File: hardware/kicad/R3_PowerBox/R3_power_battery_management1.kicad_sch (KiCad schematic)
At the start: 22 parts, among them J8 2S BATTERY / KEYED, J9 CHARGER NTC / OPTIONAL, Q2 20V N-MOS LOW-RDS / MPN TBD, Q3 20V N-MOS LOW-RDS / MPN TBD, U9 BQ28Z610DRZR

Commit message: Finalize R3 PowerBox pre-placement corrections
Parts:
- added C95: 100nF DSG D-S / TI EVM, Capacitor_SMD:C_0603_1608Metric, symbol R3_POWER_GEN:C
- added C96: 100nF CHG D-S / TI EVM, Capacitor_SMD:C_0603_1608Metric, symbol R3_POWER_GEN:C
- added C97: 100nF VC2-VC1 / CELL2, Capacitor_SMD:C_0603_1608Metric, symbol R3_POWER_GEN:C
- added C98: 100nF VC1-VSS / CELL1, Capacitor_SMD:C_0603_1608Metric, symbol R3_POWER_GEN:C
- added R100: 5.1k CHG GATE / TI EVM, Resistor_SMD:R_0603_1608Metric, symbol R3_POWER_GEN:R
- added R101: 10M CHG G-S / TI EVM, Resistor_SMD:R_0603_1608Metric, symbol R3_POWER_GEN:R
- added R98: 5.1k DSG GATE / TI EVM, Resistor_SMD:R_0603_1608Metric, symbol R3_POWER_GEN:R
- added R99: 10M DSG G-S / TI EVM, Resistor_SMD:R_0603_1608Metric, symbol R3_POWER_GEN:R
- added U11: BQ294502 SPACE ONLY / NC / DNP, Package_SON:WSON-6-1EP_2x2mm_P0.65mm_EP1x1.6mm, symbol Connector_Generic:Conn_01x07
- J9: value CHARGER NTC / OPTIONAL -> CHARGER NTC / QUIET DGND RETURN
- Q2: value 20V N-MOS LOW-RDS / MPN TBD -> 30V N-MOS DSG / MPN+FOOTPRINT TBD
- Q3: value 20V N-MOS LOW-RDS / MPN TBD -> 30V N-MOS CHG / MPN+FOOTPRINT TBD
- R90: value 100R VC2 -> 100R VC2 / KELVIN
- R91: value 100R VC1 -> 100R VC1 / KELVIN
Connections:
- net BAT_NEG_RAW: now also C98.2; no longer J9.2
- net BAT_POS_RAW: now also Q3.2 (S), C96.2, R101.2; no longer Q2.3 (D)
- net BMS_FET_COMMON: now also Q2.3 (D), Q3.3 (D), C95.2, C96.1; no longer Q2.2 (S), Q3.2 (S)
- net BMS_VC2_FILT: now also C97.1
- net DGND: now also J9.2
- net N$1: now also R92.2, U9.4 (TS1); no longer R91.2, U9.12 (VC1)
- net N$2: now also U9.7 (DSG), R98.1; no longer R92.2, U9.4 (TS1)
- net N$3: now also R100.1; no longer Q2.1 (G)
- net PACK_POS: now also Q2.2 (S), C95.1, R99.2; no longer Q3.3 (D)
- net N$4 renamed BMS_CHG_GATE
- net BMS_CHG_GATE: now also R100.2, R101.1; no longer U9.7 (DSG)
- new net BMS_DSG_GATE: Q2.1 (G), R98.2, R99.1
- new net BMS_VC1_FILT: C97.2, C98.1, R91.2, U9.12 (VC1)
- no-connect marks 0 -> 7
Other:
- moved on the sheet: C93, C94, J8, J9, Q2, Q3, R90, R91, R92, R93, R94, R95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

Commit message: Finalize R3 PowerBox pre-routing placement
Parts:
- J8: value 2S BATTERY / KEYED -> 2S BATTERY / KEYED / NTC_BMS=103AT-2
- J9: value CHARGER NTC / QUIET DGND RETURN -> NTC_CHG=103AT-2 / QUIET DGND RETURN
- Q2: value 30V N-MOS DSG / MPN+FOOTPRINT TBD -> CSD17577Q3AT 30V NMOS DSG; footprint (none) -> R3_Power:CSD17577Q3A_VSON-8_3.3x3.3mm
- Q3: value 30V N-MOS CHG / MPN+FOOTPRINT TBD -> CSD17577Q3AT 30V NMOS CHG; footprint (none) -> R3_Power:CSD17577Q3A_VSON-8_3.3x3.3mm
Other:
- moved on the sheet: R90, R96, R97

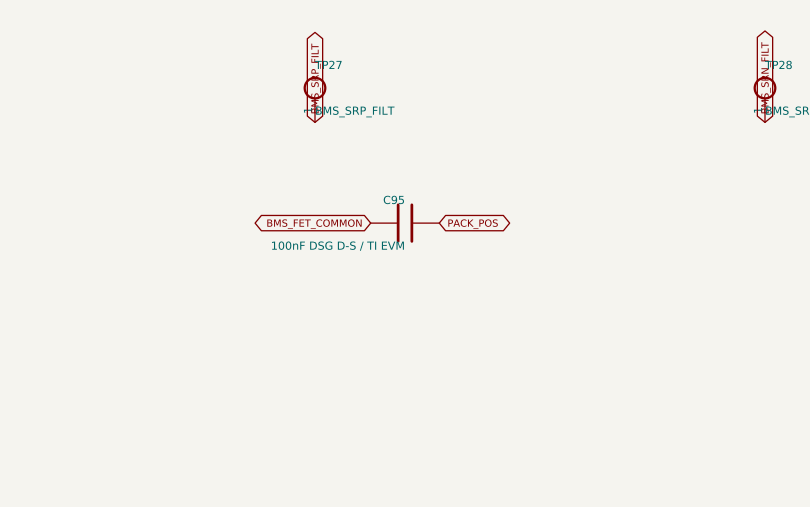
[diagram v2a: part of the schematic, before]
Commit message: Finalize R3 PowerBox user power controls
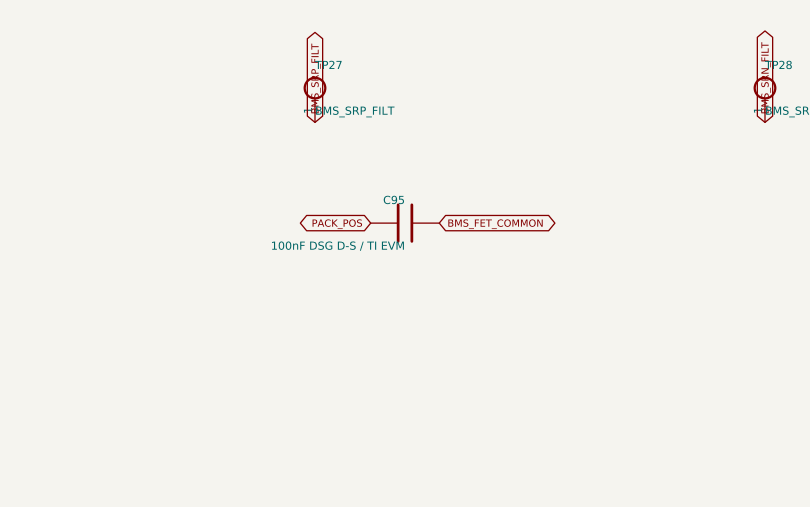
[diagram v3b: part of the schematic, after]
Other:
- moved on the sheet: C95

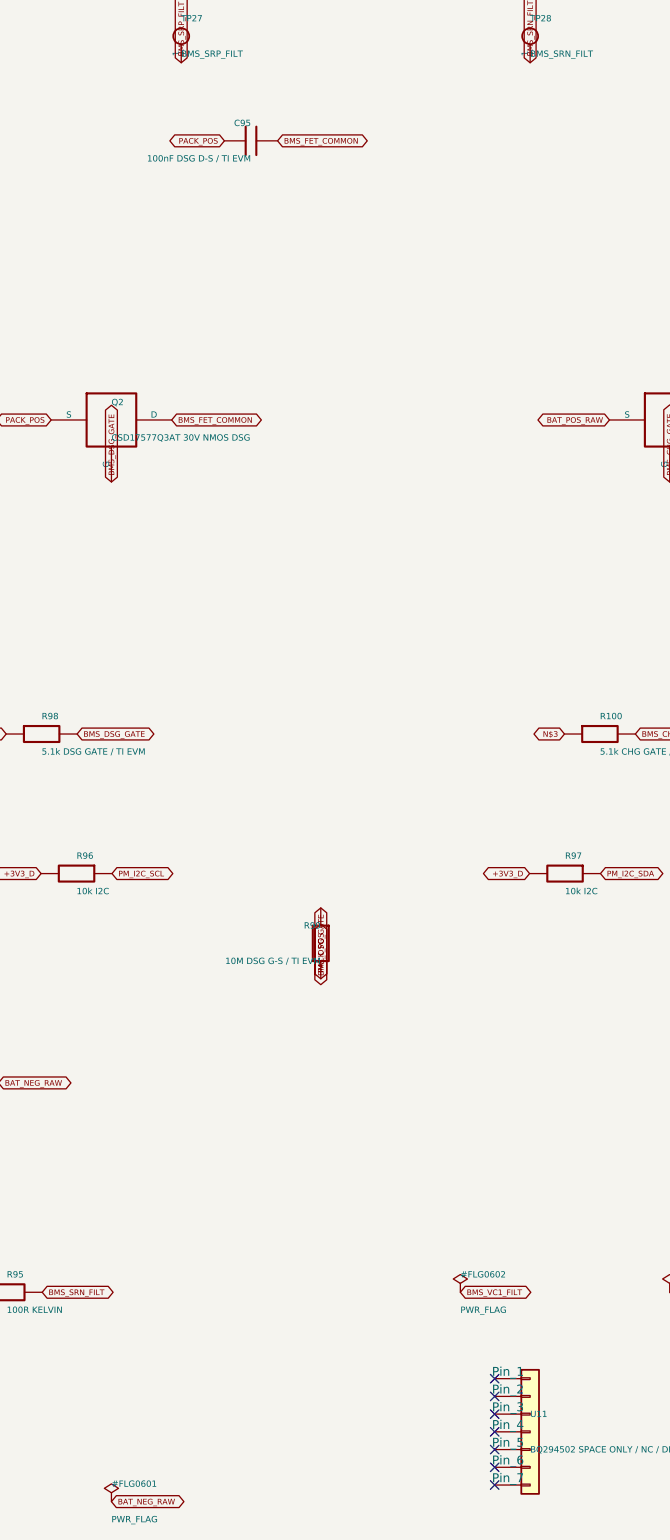
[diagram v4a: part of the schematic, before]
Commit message: Finish R3 PowerBox routing checkpoint F and verification
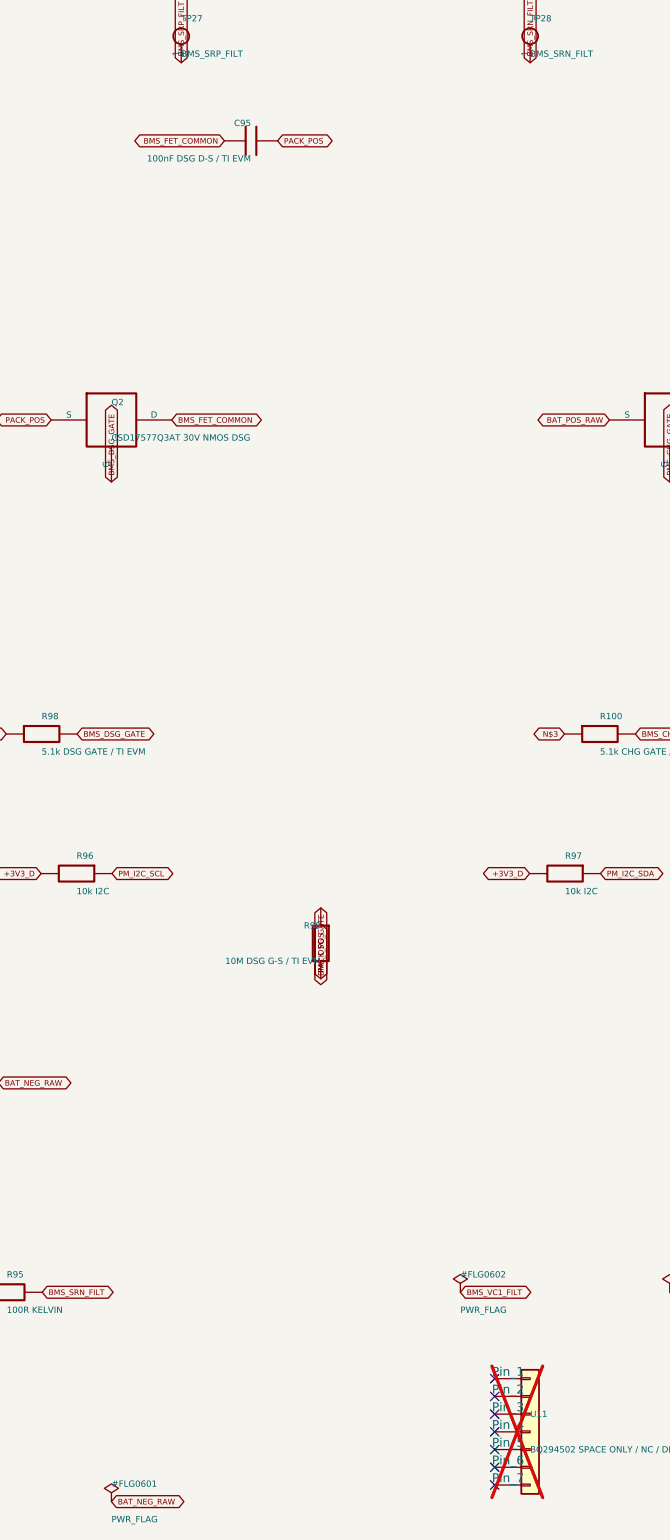
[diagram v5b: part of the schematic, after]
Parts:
- TP27, TP28: footprint TestPoint:TestPoint_Plated_Hole_D2.0mm -> TestPoint:TestPoint_Pad_D1.0mm
- U11: now not fitted
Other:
- moved on the sheet: C95

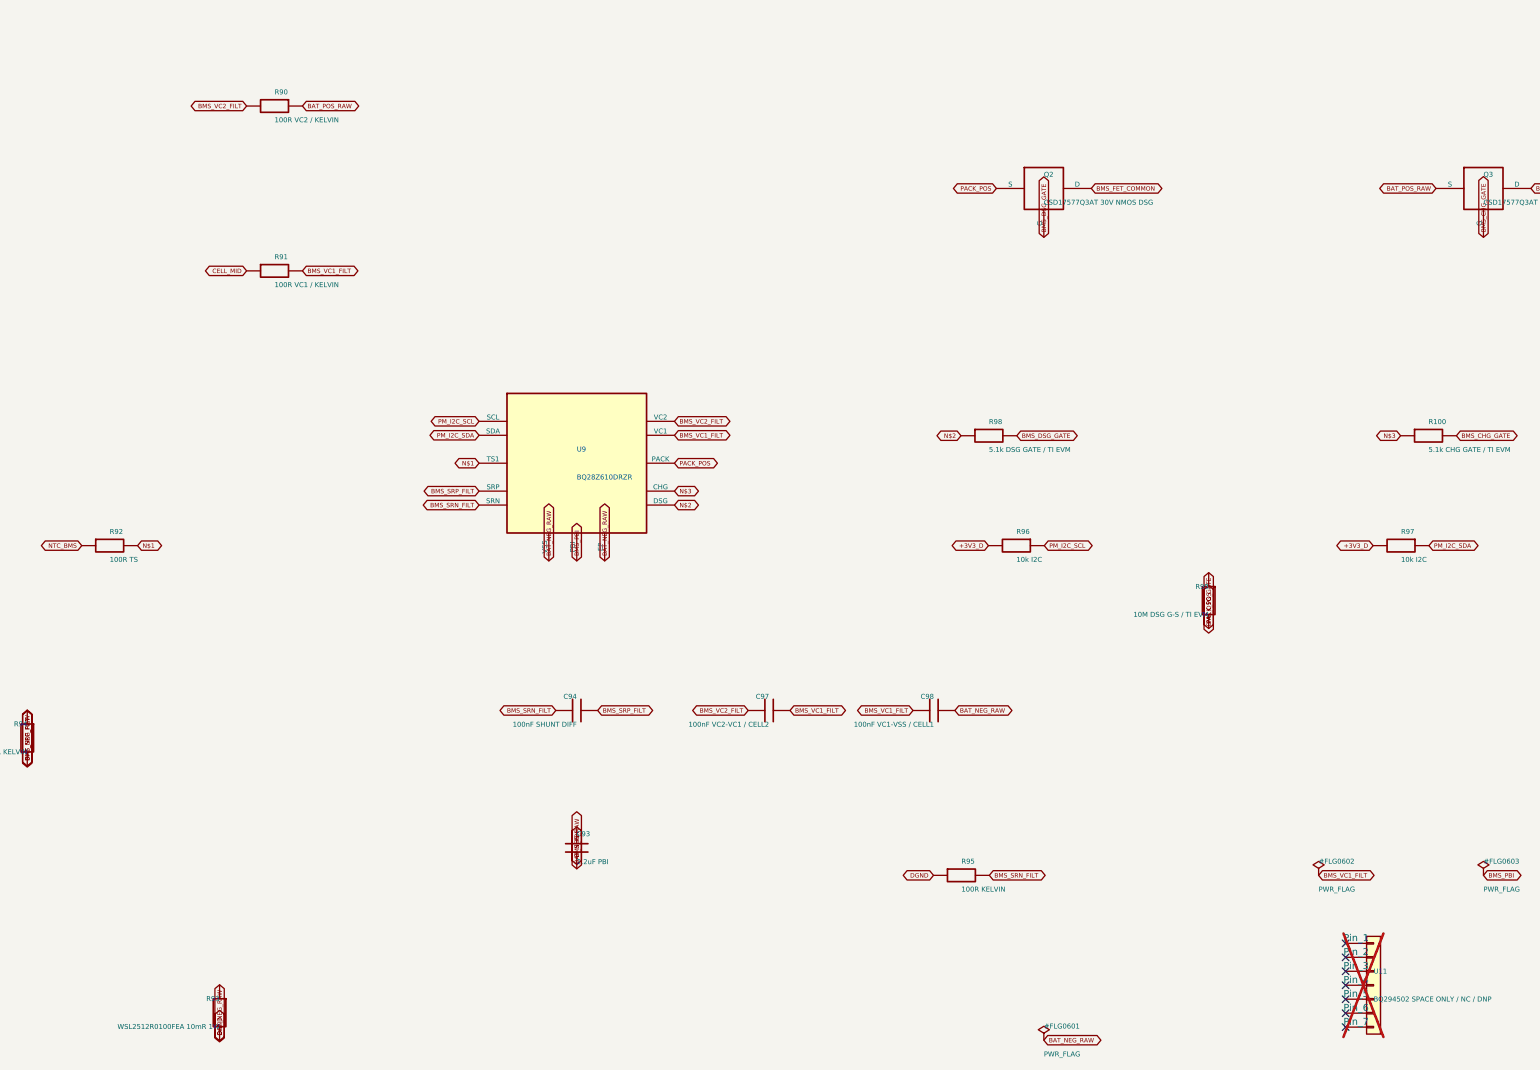
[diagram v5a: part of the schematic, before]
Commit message: Rev.A review fixes: initial schematic and component corrections
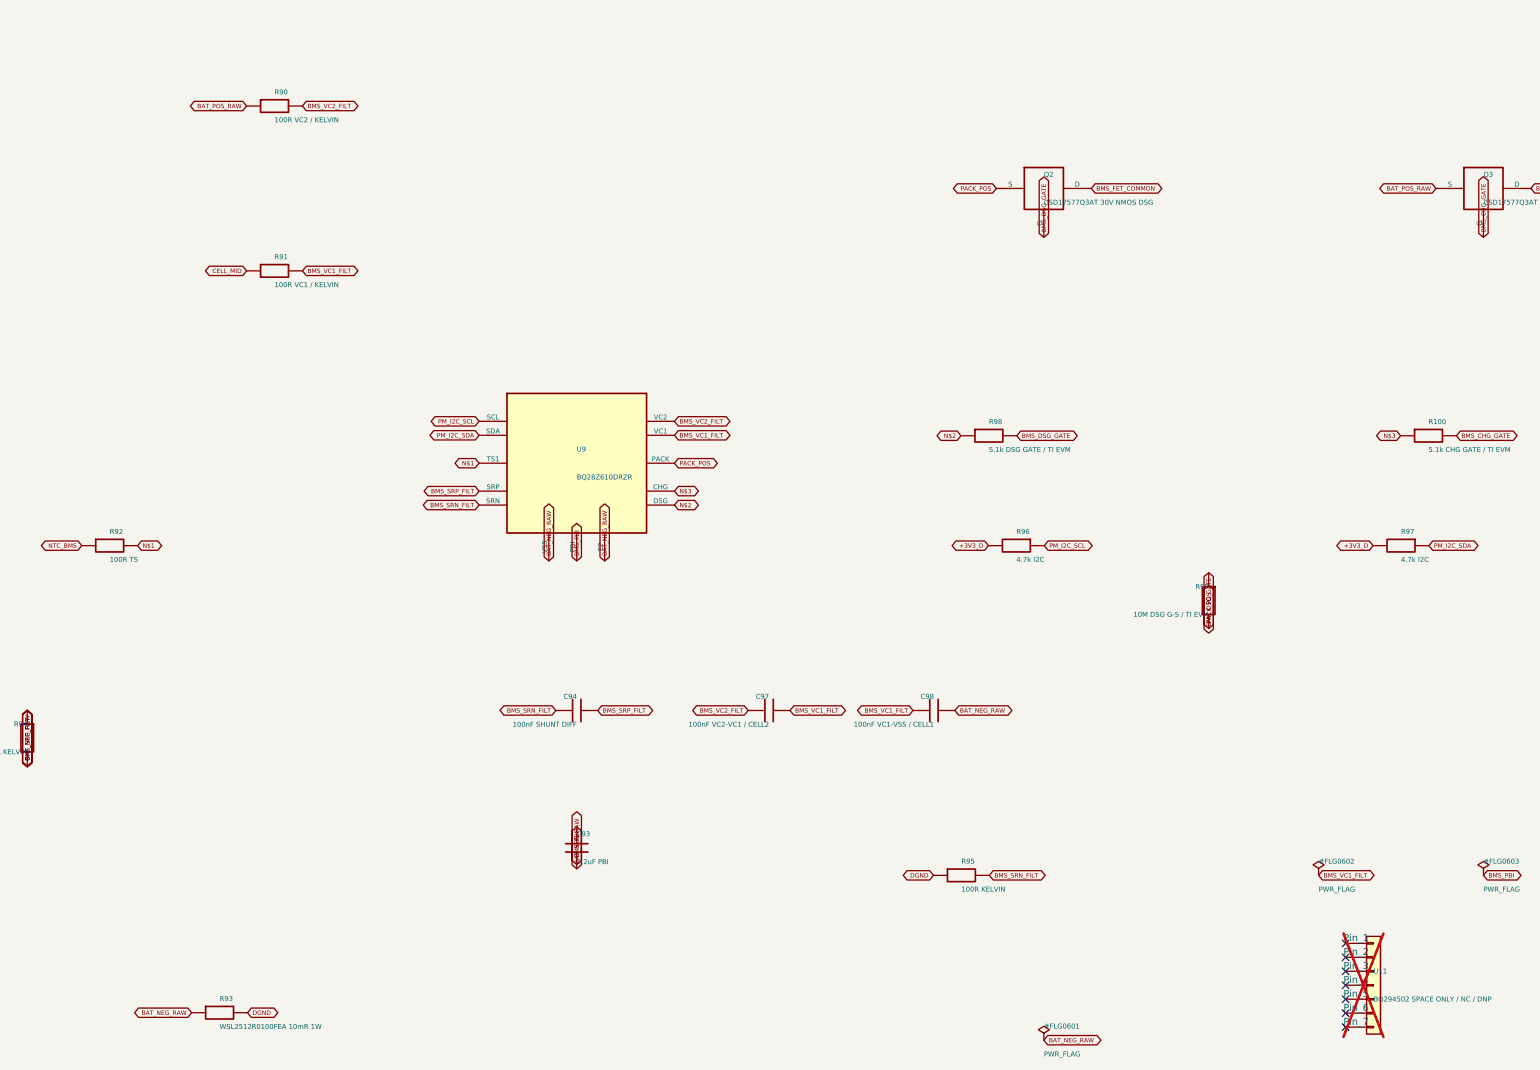
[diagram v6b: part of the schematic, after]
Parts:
- R96, R97: value 10k I2C -> 4.7k I2C
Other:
- moved on the sheet: R90, R93
